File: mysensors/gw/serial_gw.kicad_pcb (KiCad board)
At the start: 2 copper layers, 53 x 59.8 mm, 42 parts, among them CON1 AVR-ISP-10, IC1 ATMEGA328P-A, P1 USB, P2 ANTENNA, SW1 RESET, U1 RFM69HW, U2 CH340G, U3 AMS1117-3.3, X1 12MHz, X2 16MHz

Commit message: [mysensors_gw] very compact gw hw design files - initial draft
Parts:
- removed D4: MBR0520, Diodes_SMD:SOD-123
- removed F1: MF-SMDF050, myfootprints:mf-smdf050
- removed JP1: CTS, Resistors_SMD:R_0603_HandSoldering
- removed R10: 4K7, Resistors_SMD:R_0805_HandSoldering
- removed R11: 9K1, Resistors_SMD:R_0805_HandSoldering
- removed R6: 470, Resistors_SMD:R_0805_HandSoldering
- removed R7, R8, R9: 330, Resistors_SMD:R_0805_HandSoldering
- removed REF** (x4): 1pin, Connect:1pin
- removed REF**: my_logo, myfootprints:my_logo
- removed X2: 16MHz, myfootprints:ZTTCS-3
- added C11: 1u, Capacitors_SMD:C_0603_HandSoldering, F.Cu at (153.0, 90.8)
- added C12: 100n, Capacitors_SMD:C_0603_HandSoldering, F.Cu at (148.7, 104.0)
- added C13: 22u, Capacitors_SMD:C_0603_HandSoldering, F.Cu at (161.5, 92.3)
- added U4: RFM69CW, myfootprints:RFM69CW, B.Cu at (115.7, 58.2)
- C1: value 10u -> 100n; footprint Capacitors_Tantalum_SMD:TantalC_SizeT_EIA-3528 -> Capacitors_SMD:C_0805_HandSoldering
- C10: value 100n -> 1u; footprint Capacitors_SMD:C_0805_HandSoldering -> Capacitors_SMD:C_0603_HandSoldering
- C2: value 10n -> 100n
- C3, C4, C5, C6, C7: footprint Capacitors_SMD:C_0805_HandSoldering -> Capacitors_SMD:C_0603_HandSoldering
- C8: value 22u -> 1u; footprint Capacitors_Tantalum_SMD:TantalC_SizeT_EIA-3528 -> Capacitors_SMD:C_0603_HandSoldering
- C9: value 10u -> 100n; footprint Capacitors_Tantalum_SMD:TantalC_SizeT_EIA-3528 -> Capacitors_SMD:C_0603_HandSoldering
- CON1: value AVR-ISP-10 -> AVR-ISP-6; footprint Pin_Headers:Pin_Header_Straight_2x05 -> myfootprints:AVR_ISP_SMT_Small_02x03
- D1, D2, D3: footprint LEDs:LED-3MM -> LEDs:LED_0603
- IC1: value ATMEGA328P-A -> ATMEGA328P-AU; footprint Housings_QFP:TQFP-32_7x7mm_Pitch0.8mm -> Housings_DFN_QFN:QFN-32-1EP_5x5mm_Pitch0.5mm
- P1: value USB -> USB_A; footprint Connect:USB_Mini-B -> Connect:USB_A; moved to B.Cu
- P2: footprint Pin_Headers:Pin_Header_Straight_1x01 -> Pin_Headers:Pin_Header_Straight_1x01_Pitch2.54mm
- R1: footprint Resistors_SMD:R_0805_HandSoldering -> Resistors_SMD:R_0603_HandSoldering
- R2, R4: value 4K7 -> 330; footprint Resistors_SMD:R_0805_HandSoldering -> Resistors_SMD:R_0603_HandSoldering
- R3: value 9K1 -> 330; footprint Resistors_SMD:R_0805_HandSoldering -> Resistors_SMD:R_0603_HandSoldering
- R5: value 9K1 -> 56K; footprint Resistors_SMD:R_0805_HandSoldering -> Resistors_SMD:R_0603_HandSoldering
- SW1: footprint Buttons_Switches_ThroughHole:SW_PUSH_6mm -> Buttons_Switches_SMD:SW_SPST_FSMSM
- U1: value RFM69HW -> TXB0104PWR; footprint mysensors_radios:RFM69HW_SMD_Handsoldering -> Housings_SSOP:TSSOP-14_4.4x5mm_Pitch0.65mm
- U2: value CH340G -> MCP1703A-3302/MB; footprint Housings_SOIC:SOIC-16_3.9x9.9mm_Pitch1.27mm -> TO_SOT_Packages_SMD:SOT89-3_Housing
- U3: value AMS1117-3.3 -> CP2102; footprint TO_SOT_Packages_SMD:SOT-223 -> Housings_DFN_QFN:QFN-28-1EP_5x5mm_Pitch0.5mm
- X1: value 12MHz -> 16MHz
- moved P2 66.0 mm to (102.5, 52.5), turned to 0 degrees
- moved U3 61.2 mm to (99.3, 90.8)
- moved SW1 59.4 mm to (145.7, 55.8), turned to 0 degrees
- moved D1 57.8 mm to (175.5, 82.1)
- moved U1 54.2 mm to (117.4, 58.8), turned to 0 degrees
- moved R1 53.9 mm to (175.0, 76.9), turned to 0 degrees
- moved CON1 52.0 mm to (131.9, 54.1), turned to 0 degrees
- moved U2 51.0 mm to (99.1, 100.8), turned to 0 degrees
- moved D2 49.3 mm to (166.2, 93.8)
- moved C10 45.3 mm to (142.2, 108.7), turned to 0 degrees
- moved X1 40.0 mm to (108.9, 72.8), turned to 0 degrees
- moved C7 37.6 mm to (157.3, 92.3), turned to 0 degrees
- moved C4 35.9 mm to (170.6, 76.9), turned to 0 degrees
- moved P1 35.6 mm to (92.8, 94.5), turned to 90 degrees
- moved C1 32.8 mm to (158.5, 86.3), turned to 0 degrees
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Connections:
- C1 pad 1: Net-(C1-Pad1) -> +5V
- C10 pad 1: /RST -> GND
- C10 pad 2: /DTR -> +5V
- C2 pad 1: Net-(C2-Pad1) -> GND
- C2 pad 2: GND -> +5V
- C3 pad 1: +5V -> GND
- C3 pad 2: GND -> +5V
- C4 pad 2: +5V -> Net-(C4-Pad2)
- C5 pad 2: +5V -> /RST
- C6 pad 1: GND -> /RST
- C6 pad 2: Net-(C6-Pad2) -> /DTR
- C7 pad 1: GND -> +5V
- C7 pad 2: /RST -> GND
- C8 pad 1: +3V3 -> +5V
- C9 pad 1: +3V3 -> GND
- C9 pad 2: GND -> +3V3
- CON1 pad 1: /MOSI -> /MISO
- CON1 pad 3: Net-(CON1-Pad3) -> /SCK
- CON1 pad 4: GND -> /MOSI
- IC1 pad 1: Net-(IC1-Pad1) -> (no net)
- IC1 pad 10: Net-(IC1-Pad10) -> (no net)
- IC1 pad 11: Net-(IC1-Pad11) -> (no net)
- IC1 pad 12: Net-(IC1-Pad12) -> (no net)
- IC1 pad 13: Net-(IC1-Pad13) -> (no net)
- IC1 pad 19: Net-(IC1-Pad19) -> (no net)
- IC1 pad 2: Net-(IC1-Pad2) -> (no net)
- IC1 pad 20: Net-(C6-Pad2) -> Net-(C4-Pad2)
- IC1 pad 22: Net-(IC1-Pad22) -> (no net)
- IC1 pad 26: Net-(IC1-Pad26) -> (no net)
- IC1 pad 27: Net-(IC1-Pad27) -> (no net)
- IC1 pad 28: Net-(IC1-Pad28) -> (no net)
- IC1 pad 30: /SerialTx -> /SER_TX
- IC1 pad 31: /SerialRx -> /SER_RX
- IC1 pad 9: Net-(IC1-Pad9) -> (no net)
- P1 pad 1: Net-(F1-Pad1) -> +5V
- P1 pad 4: Net-(P1-Pad4) -> GND
- R2 pad 1: Net-(R2-Pad1) -> Net-(D1-Pad2)
- R2 pad 2: /MOSI -> /GW_RX_LED
- R3 pad 1: Net-(R2-Pad1) -> Net-(D2-Pad2)
- R3 pad 2: GND -> /GW_TX_LED
- R4 pad 1: Net-(R4-Pad1) -> Net-(D3-Pad2)
- R4 pad 2: /SS -> /GW_ERR_LED
- R5 pad 1: Net-(R4-Pad1) -> Net-(R5-Pad1)
- R5 pad 2: GND -> +3V3
- U1 pad 1: Net-(U1-Pad1) -> +3V3
- U1 pad 10: Net-(P2-Pad1) -> (no net)
- U1 pad 11: GND -> /SCK
- U1 pad 12: Net-(R10-Pad1) -> /MOSI
- U1 pad 13: /MISO -> /SS
- U1 pad 14: Net-(R2-Pad1) -> +5V
- U1 pad 2: /INT -> Net-(R5-Pad1)
- U1 pad 5: Net-(U1-Pad5) -> (no net)
- U1 pad 6: Net-(U1-Pad6) -> (no net)
- U1 pad 7: Net-(U1-Pad7) -> GND
- U1 pad 9: GND -> (no net)
- U2 pad 2: /SerialTx -> +5V
- U2 pad 3: /SerialRx -> +3V3
- U3 pad 1: GND -> (no net)
- U3 pad 2: +3V3 -> (no net)
- U3 pad 3: +5V -> GND
- U3 pad 4: (no net) -> Net-(P1-Pad3)
- X1 pad 1: Net-(U2-Pad7) -> Net-(IC1-Pad8)
- X1 pad 2: Net-(U2-Pad8) -> GND
- X1 pad 3: GND -> Net-(IC1-Pad7)
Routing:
- net GND: track 284.6 -> 0.00 mm
- net +5V: track 128.9 -> 0.00 mm, vias 5 -> 0
- net /RST: track 68.5 -> 0.00 mm, vias 2 -> 0
- net /SCK: track 45.2 -> 0.00 mm, vias 3 -> 0
- net /MISO: track 43.1 -> 0.00 mm, vias 3 -> 0
- net +3V3: track 38.6 -> 0.00 mm, vias 2 -> 0
- net /INT: track 33.4 -> 0.00 mm, vias 2 -> 0
- net /SerialRx: track 29.3 -> 0.00 mm, vias 2 -> 0
- net /MOSI: track 27.9 -> 0.00 mm, vias 1 -> 0
- net /SerialTx: track 27.3 -> 0.00 mm, vias 2 -> 0
- net Net-(P1-Pad2): track 22.3 -> 0.00 mm
- net Net-(R2-Pad1): track 20.8 -> 0.00 mm, vias 2 -> 0
- net Net-(P1-Pad3): track 20.4 -> 0.00 mm
- net Net-(R4-Pad1): track 16.4 -> 0.00 mm
- net /GW_RX_LED: track 12.6 -> 0.00 mm
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- removed copper zone on B.Cu, net GND
- removed copper zone on F.Cu, net GND
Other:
- board outline removed
- net class Default: clearance 0.3 -> 0.2; trace_width 0.4 -> 0.25
- rule trace_clearance: 0.3 -> 0.2
- rule trace_min: 0.4 -> 0.2
- board text removed: "+"
- board text removed: "Antenna Length: 433 MHz -> 165 mm 868 MHz -> 82 mm 915 MHz -> 78 mm"
- board text removed: "MOSI RST SCK MISO"
- board text removed: "Mysensors RFM69 Gateway Rev1.0"

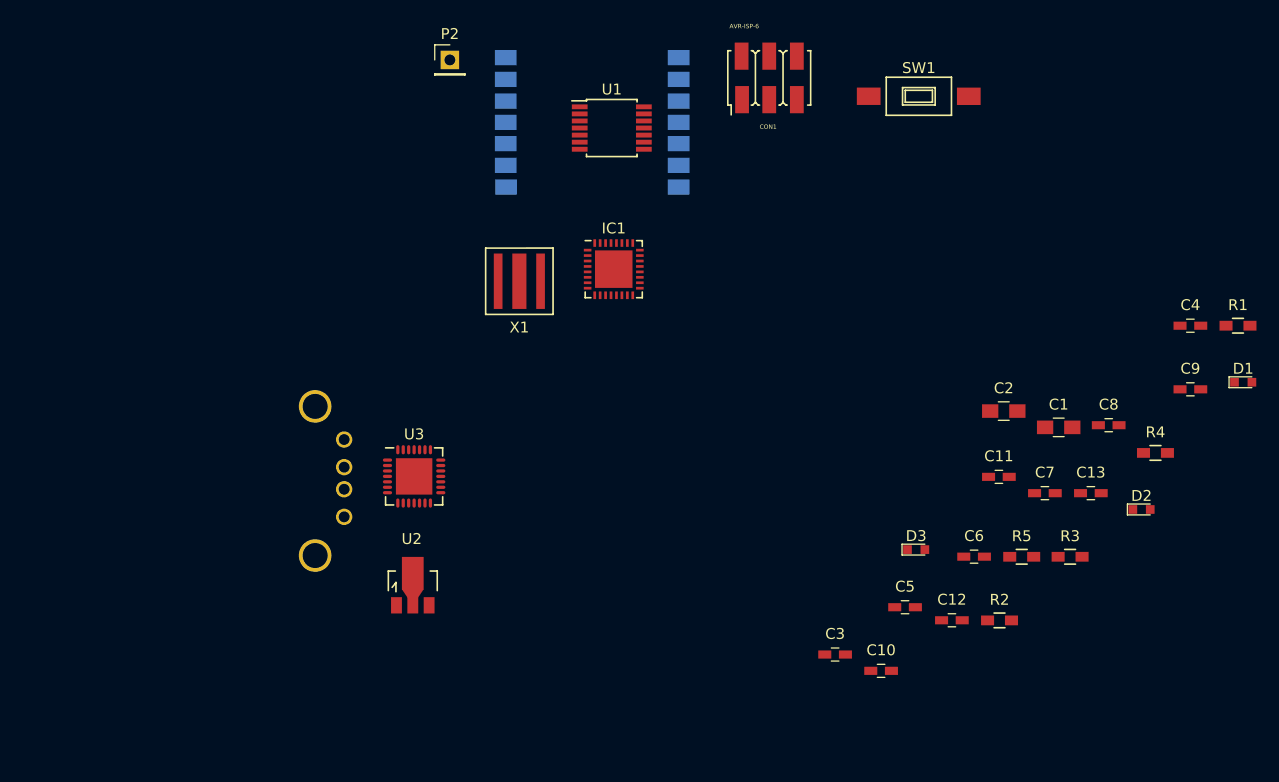
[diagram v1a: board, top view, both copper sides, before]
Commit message: [mysensors_gw] pcb routing - 1st pass
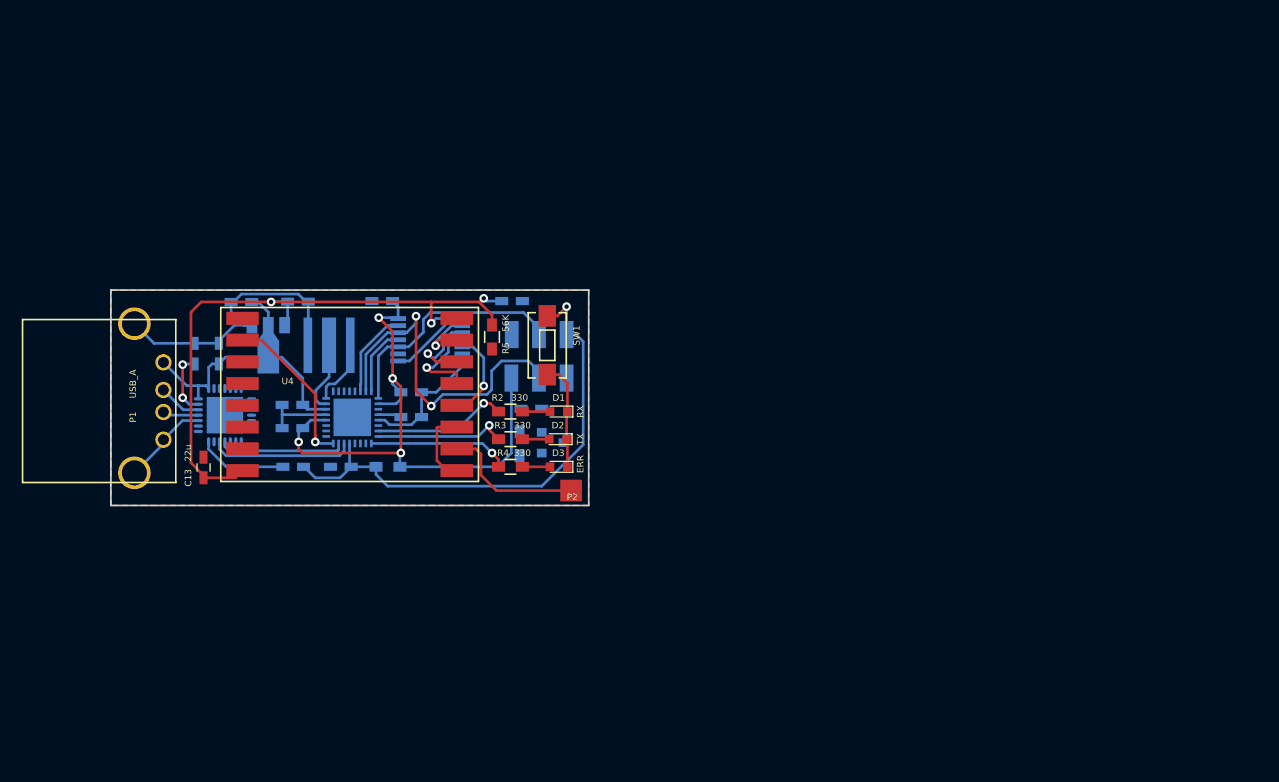
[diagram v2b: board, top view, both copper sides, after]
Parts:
- added C14: 100n, Capacitors_SMD:C_0603_HandSoldering, B.Cu at (110.0, 84.6)
- added R6: 1K, Resistors_SMD:R_0603_HandSoldering, B.Cu at (109.0, 87.8)
- added U5: ATSHA204A, TO_SOT_Packages_SMD:SOT-23, B.Cu at (112.0, 87.7)
- C1, C2: footprint Capacitors_SMD:C_0805_HandSoldering -> Capacitors_SMD:C_0603_HandSoldering; moved to B.Cu
- C10, C11, C12, C3, C4, C5, C6, C7, C8, C9, CON1, R1, U3, X1: moved to B.Cu
- D1: value GW_RX -> RX
- D2: value GW_TX -> TX
- D3: value GW_ERR -> ERR
- IC1: value ATMEGA328P-AU -> ATMEGA328P-MU; moved to B.Cu
- P1: moved to F.Cu
- P2: footprint Pin_Headers:Pin_Header_Straight_1x01_Pitch2.54mm -> myfootprints:1pin_smd_2mm
- SW1: value RESET -> TACTM-35N-F; footprint Buttons_Switches_SMD:SW_SPST_FSMSM -> Buttons_Switches_SMD:SW_SPST_EVQPE1
- U1: value TXB0104PWR -> TXB0104; moved to B.Cu
- U2: value MCP1703A-3302/MB -> MCP1703A-3302; moved to B.Cu
- U4: value RFM69CW -> RFM69HW; footprint myfootprints:RFM69CW -> mysensors_radios:RFM69HW_SMD_Handsoldering; moved to F.Cu
- moved C13 81.6 mm to (79.9, 90.0), turned to 90 degrees
- moved C8 80.6 mm to (83.4, 74.8), turned to 180 degrees
- moved R1 79.2 mm to (96.9, 89.9), turned to 180 degrees
- moved C12 73.8 mm to (79.1, 79.5), turned to 90 degrees
- moved C4 72.1 mm to (99.0, 85.3), turned to 180 degrees
- moved C1 70.5 mm to (88.1, 84.2), turned to 180 degrees
- moved C10 67.5 mm to (81.3, 79.5), turned to 270 degrees
- moved C11 66.4 mm to (88.6, 74.7)
- moved C7 63.4 mm to (96.3, 74.7), turned to 180 degrees
- moved C6 63.2 mm to (88.1, 89.9), turned to 180 degrees
- moved D1 63.0 mm to (112.6, 84.8), turned to 180 degrees
- moved C9 62.9 mm to (108.3, 74.7), turned to 180 degrees
- moved R4 59.3 mm to (108.1, 89.9), turned to 180 degrees
- moved C2 54.5 mm to (99.0, 83.1), turned to 180 degrees
- moved C3 54.1 mm to (88.1, 86.4)
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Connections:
- IC1 pad 26: (no net) -> /ATSHA204A
- U1 pad 10: (no net) -> /SCK
- U1 pad 11: /SCK -> /MISO
- U1 pad 5: (no net) -> Net-(U1-Pad5)
- U4 pad 1: Net-(P2-Pad1) -> (no net)
- U4 pad 10: (no net) -> Net-(P2-Pad1)
- U4 pad 11: (no net) -> GND
- U4 pad 12: (no net) -> Net-(U1-Pad5)
- U4 pad 13: (no net) -> Net-(U1-Pad4)
- U4 pad 14: GND -> Net-(U1-Pad3)
- U4 pad 2: +3V3 -> /INT
- U4 pad 3: GND -> (no net)
- U4 pad 5: Net-(U1-Pad3) -> (no net)
- U4 pad 6: Net-(U1-Pad4) -> (no net)
- U4 pad 7: Net-(R5-Pad1) -> (no net)
- U4 pad 8: /MISO -> +3V3
- U4 pad 9: /INT -> GND
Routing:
- net +5V: track 0.00 -> 80.4 mm, vias 0 -> 4
- net GND: track 0.00 -> 70.7 mm
- net +3V3: track 0.00 -> 66.3 mm, vias 0 -> 3
- net /RST: track 0.00 -> 47.5 mm, vias 0 -> 1
- net /MOSI: track 0.00 -> 32.3 mm, vias 0 -> 2
- net /SCK: track 0.00 -> 22.2 mm
- net /INT: track 0.00 -> 14.7 mm, vias 0 -> 1
- net Net-(P2-Pad1): track 0.00 -> 14.1 mm
- net /SER_TX: track 0.00 -> 13.3 mm
- net /GW_ERR_LED: track 0.00 -> 13.0 mm, vias 0 -> 1
- net /GW_RX_LED: track 0.00 -> 12.4 mm, vias 0 -> 1
- net /GW_TX_LED: track 0.00 -> 12.2 mm, vias 0 -> 1
- net /SER_RX: track 0.00 -> 11.7 mm
- net Net-(U1-Pad4): track 0.00 -> 8.68 mm, vias 0 -> 1
- net Net-(U1-Pad5): track 0.00 -> 8.33 mm, vias 0 -> 1
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- added copper zone on B.Cu, net GND
- added copper zone on F.Cu, net GND
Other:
- board outline added: 43.9 x 19.8 mm

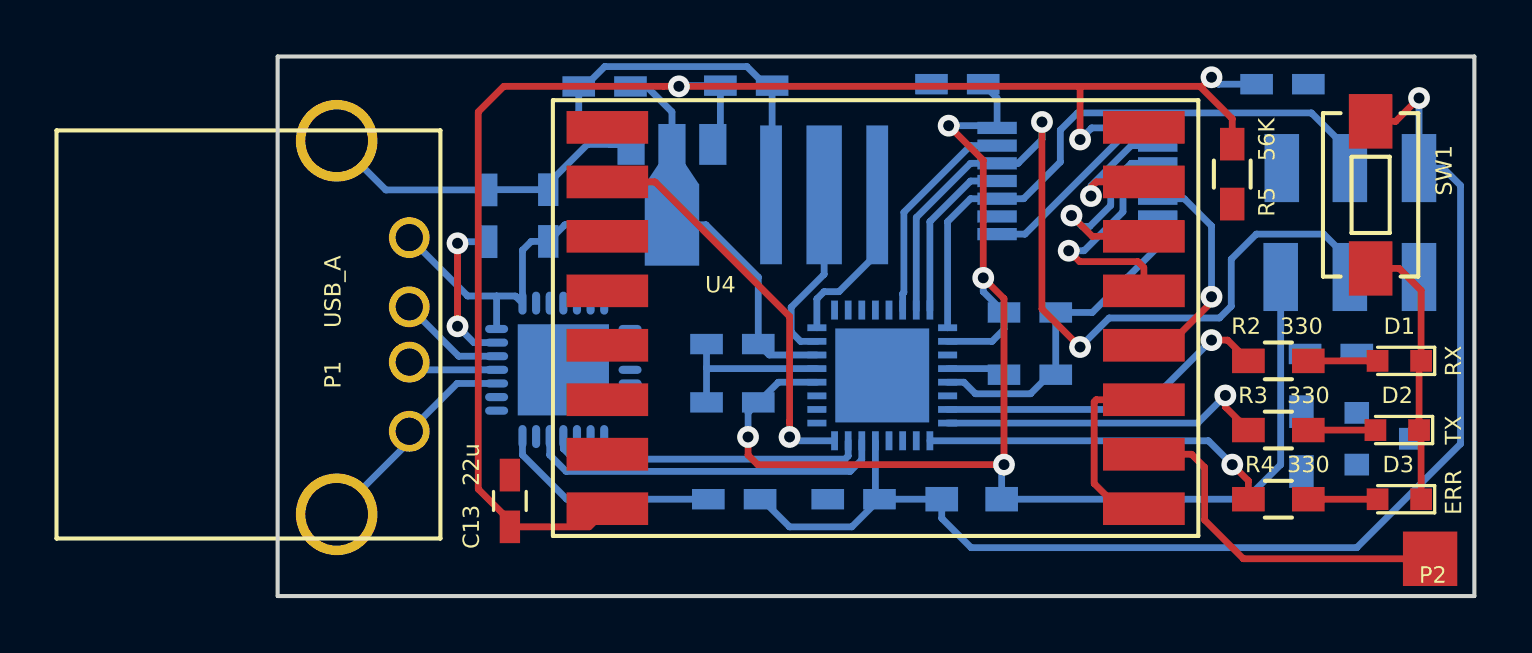
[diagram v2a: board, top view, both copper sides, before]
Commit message: [mysensors_gw] pcb routing - 2nd pass
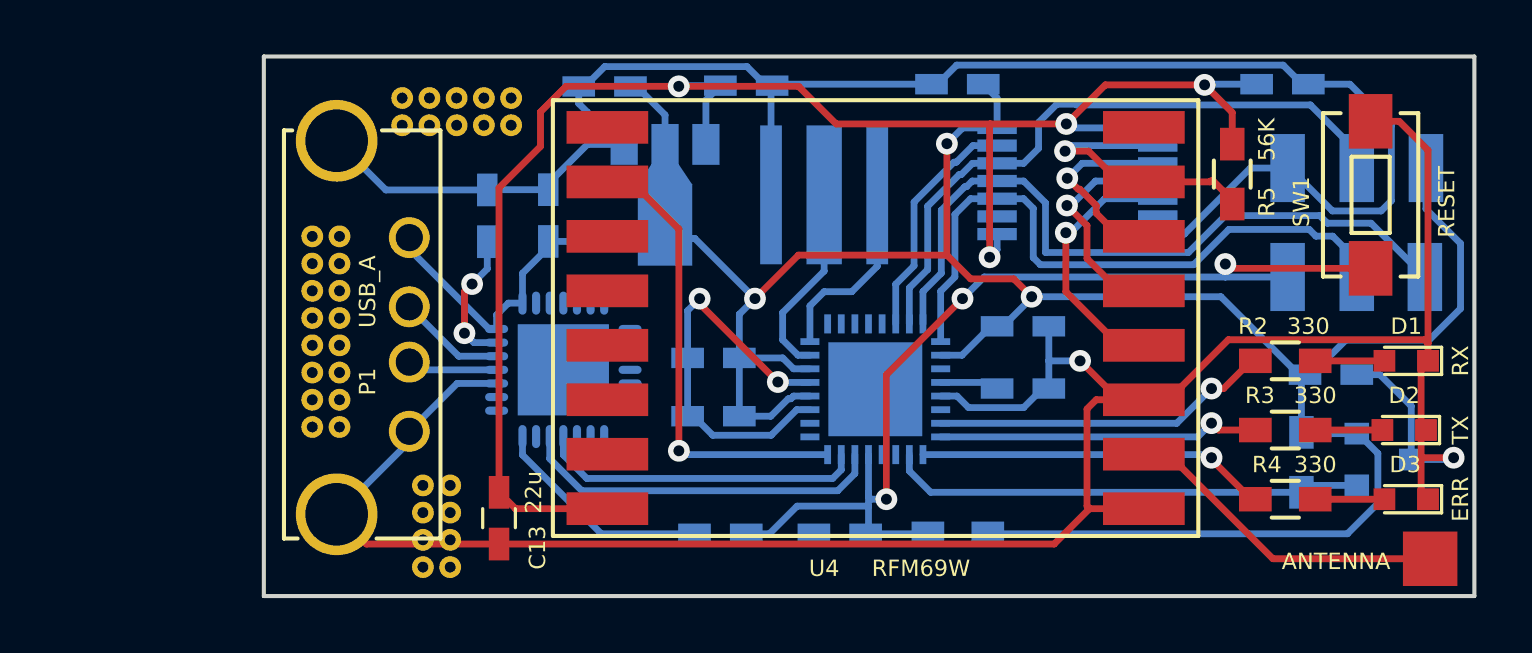
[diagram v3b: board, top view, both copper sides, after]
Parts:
- added REF**: 1pin, myfootprints:1pin, F.Cu at (73.6, 87.3)
- added REF**: 1pin, myfootprints:1pin, F.Cu at (72.6, 83.3)
- added REF**: 1pin, myfootprints:1pin, F.Cu at (73.6, 82.3)
- added REF**: 1pin, myfootprints:1pin, F.Cu at (72.6, 82.3)
- added REF**: 1pin, myfootprints:1pin, F.Cu at (73.6, 81.3)
- added REF**: 1pin, myfootprints:1pin, F.Cu at (72.6, 81.3)
- added REF**: 1pin, myfootprints:1pin, F.Cu at (73.6, 80.3)
- added REF**: 1pin, myfootprints:1pin, F.Cu at (72.6, 80.3)
- added REF**: 1pin, myfootprints:1pin, F.Cu at (77.7, 92.4)
- added REF**: 1pin, myfootprints:1pin, F.Cu at (76.7, 92.4)
- added REF**: 1pin, myfootprints:1pin, F.Cu at (77.7, 91.4)
- added REF**: 1pin, myfootprints:1pin, F.Cu at (72.6, 87.3)
- added REF**: 1pin, myfootprints:1pin, F.Cu at (76.7, 91.4)
- added REF**: 1pin, myfootprints:1pin, F.Cu at (77.7, 90.4)
- added REF**: 1pin, myfootprints:1pin, F.Cu at (76.7, 90.4)
- added REF**: 1pin, myfootprints:1pin, F.Cu at (77.7, 89.4)
- added REF**: 1pin, myfootprints:1pin, F.Cu at (76.7, 89.4)
- added REF**: 1pin, myfootprints:1pin, F.Cu at (79.9, 76.2)
- added REF**: 1pin, myfootprints:1pin, F.Cu at (78.9, 76.2)
- added REF**: 1pin, myfootprints:1pin, F.Cu at (77.9, 76.2)
- added REF**: 1pin, myfootprints:1pin, F.Cu at (76.9, 76.2)
- added REF**: 1pin, myfootprints:1pin, F.Cu at (75.9, 76.2)
- added REF**: 1pin, myfootprints:1pin, F.Cu at (73.6, 86.3)
- added REF**: 1pin, myfootprints:1pin, F.Cu at (79.9, 75.2)
- added REF**: 1pin, myfootprints:1pin, F.Cu at (78.9, 75.2)
- added REF**: 1pin, myfootprints:1pin, F.Cu at (77.9, 75.2)
- added REF**: 1pin, myfootprints:1pin, F.Cu at (76.9, 75.2)
- added REF**: 1pin, myfootprints:1pin, F.Cu at (75.9, 75.2)
- added REF**: 1pin, myfootprints:1pin, F.Cu at (72.6, 86.3)
- added REF**: 1pin, myfootprints:1pin, F.Cu at (73.6, 85.3)
- added REF**: 1pin, myfootprints:1pin, F.Cu at (72.6, 85.3)
- added REF**: 1pin, myfootprints:1pin, F.Cu at (73.6, 84.3)
- added REF**: 1pin, myfootprints:1pin, F.Cu at (72.6, 84.3)
- added REF**: 1pin, myfootprints:1pin, F.Cu at (73.6, 83.3)
- added REF***: OSHW-Logo_5.7x6mm_SilkScreen, Symbols:OSHW-Logo_5.7x6mm_SilkScreen, B.Cu at (102.6, 89.7)
- P1: footprint Connect:USB_A -> myfootprints:USB_A
- SW1: value TACTM-35N-F -> RESET
- U4: value RFM69HW -> RFM69W
- moved C5 1.37 mm to (92.0, 91.2)
- moved C6 1.37 mm to (87.6, 91.2)
- moved R1 1.37 mm to (96.3, 91.2)
- moved C1 0.86 mm to (87.4, 84.7)
- moved C3 0.86 mm to (87.4, 86.9)
- moved C14 0.76 mm to (110.0, 85.3)
- moved R6 0.76 mm to (109.0, 88.6)
- moved U5 0.76 mm to (112.0, 88.5)
- moved C13 0.75 mm to (79.5, 90.6), turned to 270 degrees
- moved C4 0.57 mm to (98.7, 85.9)
- moved C2 0.57 mm to (98.7, 83.6)
- moved IC1 0.57 mm to (93.3, 85.9)
- moved CON1 0.25 mm to (111.0, 79.8), turned to 180 degrees
- moved D2 0.25 mm to (112.7, 87.4)
- moved U2 0.25 mm to (85.6, 78.7)
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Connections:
- net /INT renamed /RFM69W_INT
- net /SS renamed /RFM69W_SS
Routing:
- net GND: track 70.7 -> 168.3 mm, vias 0 -> 4
- net +5V: track 80.4 -> 105.2 mm, vias 4 -> 3
- net /MISO: track 6.33 -> 26.3 mm
- net /ATSHA204A: track 0.00 -> 17.5 mm
- net /RST: track 47.5 -> 37.7 mm, vias 1 -> 3
- net /MOSI: track 32.3 -> 23.8 mm, vias 2 -> 0
- net Net-(R5-Pad1): track 5.79 -> 10.6 mm
- net +3V3: track 66.3 -> 62.5 mm, vias 3 -> 4
- net /RFM69W_INT: track 14.7 -> 17.0 mm
- net Net-(P2-Pad1): track 14.1 -> 12.1 mm
- net Net-(U1-Pad5): track 8.33 -> 9.74 mm
- net /SCK: track 22.2 -> 23.6 mm
- net Net-(IC1-Pad8): track 6.12 -> 7.01 mm
- net Net-(C12-Pad1): track 5.85 -> 5.03 mm
- net /RFM69W_SS: track 8.05 -> 8.66 mm
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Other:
- board size 43.9 x 19.8 mm -> 44.5 x 19.8 mm
- board text added: "+5V"
- board text added: "GND"
- board text added: "MISO"
- board text added: "MOSI"
- board text added: "RST"
- board text added: "Rev. 0.1"
- board text added: "SCK"
